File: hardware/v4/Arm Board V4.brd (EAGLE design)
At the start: 127 x 50.8 mm, 44 parts, among them IC2 REG1118, U1 SN74LS241DW, U2 XBEE-1B3, U3 LSM9DS0

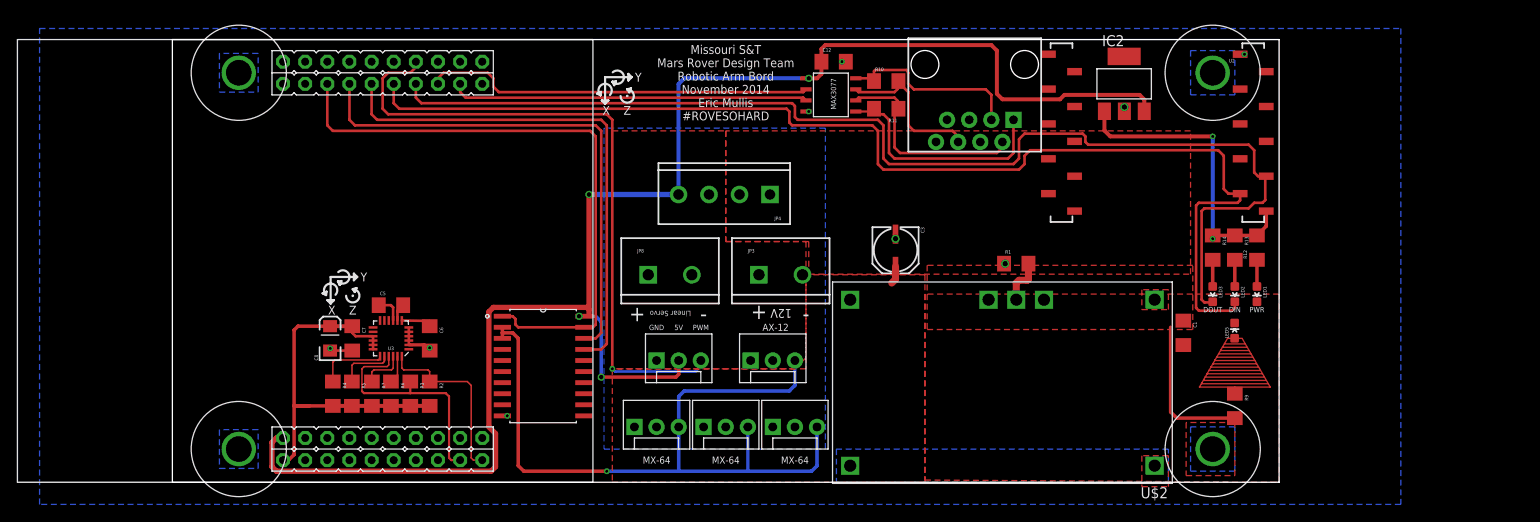
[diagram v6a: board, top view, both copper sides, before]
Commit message: Pour and Spacing changes
Worked on spacing the pours and power connectors so they made sense for
pluggable screw terminals.
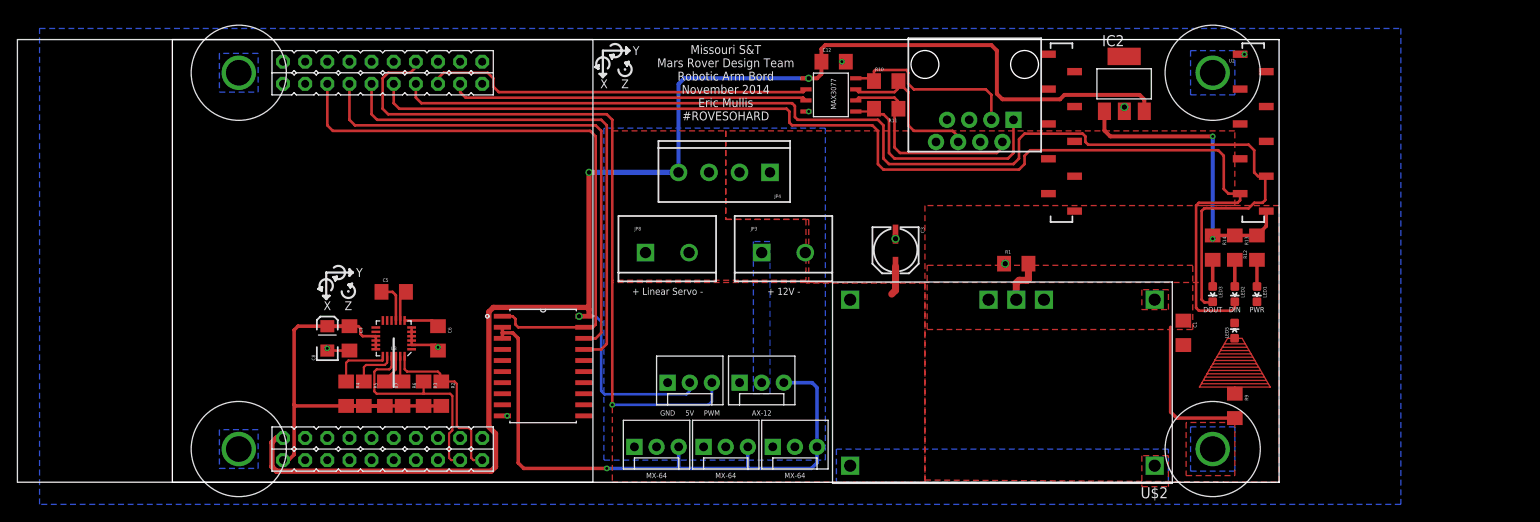
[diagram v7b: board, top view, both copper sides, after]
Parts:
- moved JP7 2.84 mm to (56.8, 11.4)
- moved JP12 2.84 mm to (65.1, 11.4)
- moved JP8 2.56 mm to (54.3, 26.4)
- moved JP3 2.56 mm to (67.6, 26.4)
- moved JP4 2.54 mm to (68.6, 35.6)
- moved JP10 2.29 mm to (53.0, 4.06)
- moved JP11 2.29 mm to (68.9, 4.06)
- moved JP9 2.29 mm to (61.0, 4.06)
- moved C5 1.56 mm to (25.4, 21.8)
- moved R3 1.52 mm to (28.8, 10.2)
- moved R4 1.52 mm to (19.9, 10.2)
- moved R7 1.49 mm to (24.4, 10.2)
- moved R5 1.37 mm to (22.0, 10.2)
- moved R2 1.33 mm to (30.9, 10.2)
- moved R6 1.33 mm to (26.4, 10.2)
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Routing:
- net DDATA_1: track 87.6 -> 70.1 mm
- net LA_PWM: track 75.1 -> 81.8 mm
- net +3V3: track 45.0 -> 49.1 mm
- net GND: track 14.6 -> 11.7 mm
- net +5V: track 182.5 -> 184.9 mm, vias 4 -> 3
- net SCL: track 26.8 -> 24.9 mm
- net SDO_G: track 5.10 -> 3.42 mm
- net N$11: track 2.03 -> 3.55 mm
- net N$10: track 3.26 -> 4.71 mm
- net 14.8V: track 2.09 -> 3.36 mm
- net CS_XM: track 6.38 -> 5.27 mm
- net CS_G: track 8.04 -> 6.94 mm
- net SDA: track 20.5 -> 19.8 mm
- added copper zone on layer 16, net +12V
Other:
- board text added: "+ 12V -"
- board text added: "+ Linear Servo -"
- board text removed: "+"
- board text removed: "-"
- board text removed: "12V"
- board text removed: "Linear Servo"

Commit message: Added a few capacitors
Added capacitors on voltage supplies and regulator.
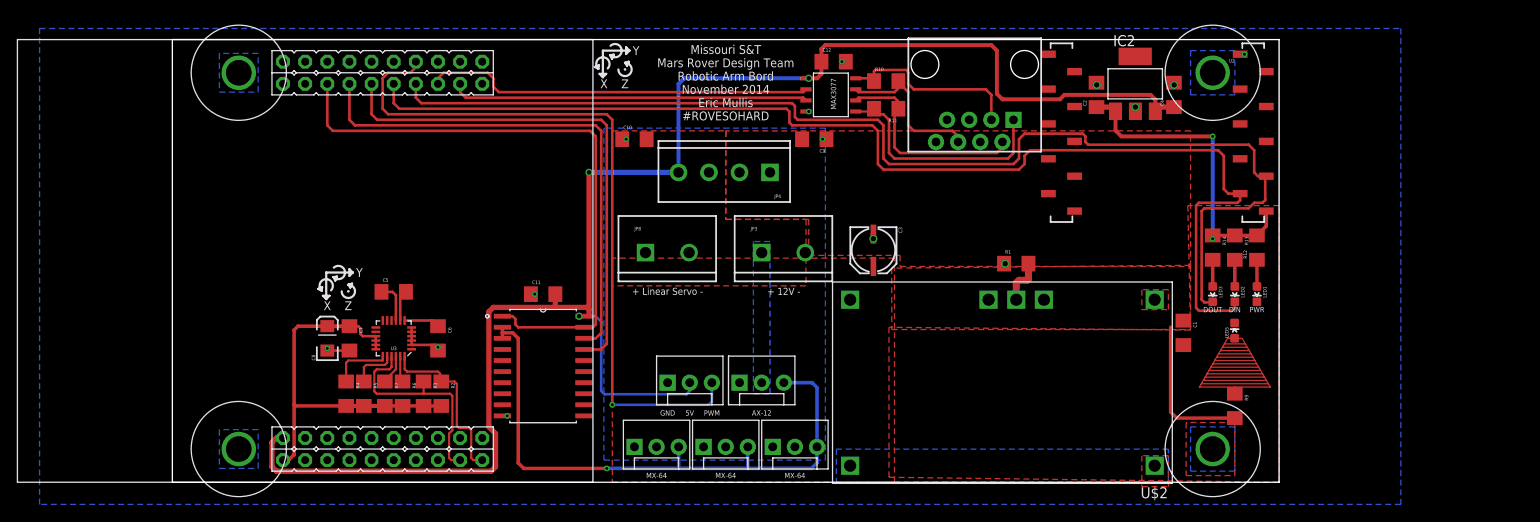
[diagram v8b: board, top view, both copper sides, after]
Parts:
- added C10, C11, C2, C4, C9: .1uF, SparkFun-Capacitors:1206
- R9: value 1k -> 1.5k
- moved C3 2.54 mm to (80.6, 26.7)
- moved IC2 1.27 mm to (110.5, 45.7)
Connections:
- net +12V: now also C10.2
- net +3.3V: now also C2.1
- net +5V: now also C11.2, C4.1
- net GND: now also C10.1, C11.1, C2.2, C4.2, C9.1
- net VIN: now also C9.2
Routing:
- net +5V: track 184.9 -> 190.0 mm
- net 14.8V: track 3.36 -> 0.00 mm
- net GND: track 11.7 -> 13.2 mm, vias 9 -> 14
- net +3.3V: track 35.4 -> 36.5 mm
